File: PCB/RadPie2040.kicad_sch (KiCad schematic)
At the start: 42 parts, among them J1 USB_C_Receptacle_USB2.0, J2 SWD, J6 Conn_01x16, J7 Conn_01x16, SW1 SW_BOOTSEL, SW2 SW_RESET, U1 W25Q128JVSIQ, U2 RP2040, U4 XC6206PxxxMR-Regulator_Linear, X1 12MHz

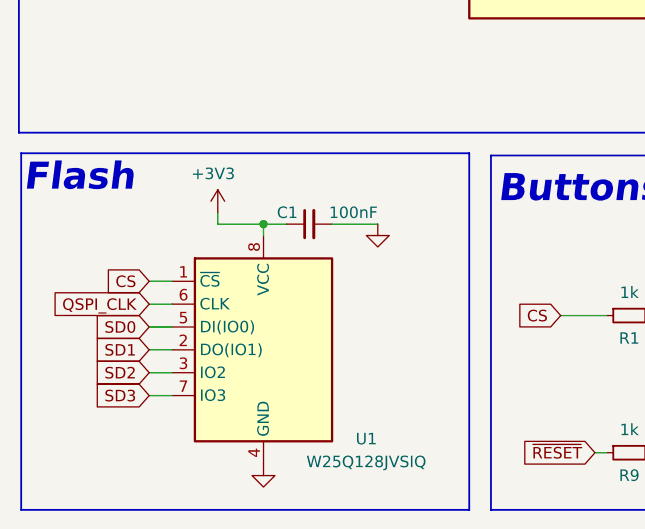
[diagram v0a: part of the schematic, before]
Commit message: Add pull-up for Flash, just in case
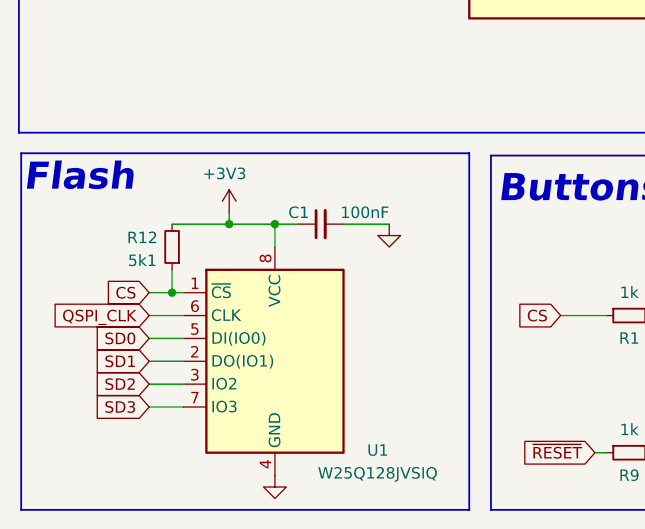
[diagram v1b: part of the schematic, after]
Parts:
- added R12: 5k1, Resistor_SMD:R_0402_1005Metric, symbol Device:R_Small
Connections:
- net +3V3: now also R12.2
- net CS: now also R12.1
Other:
- moved on the sheet: C1, U1

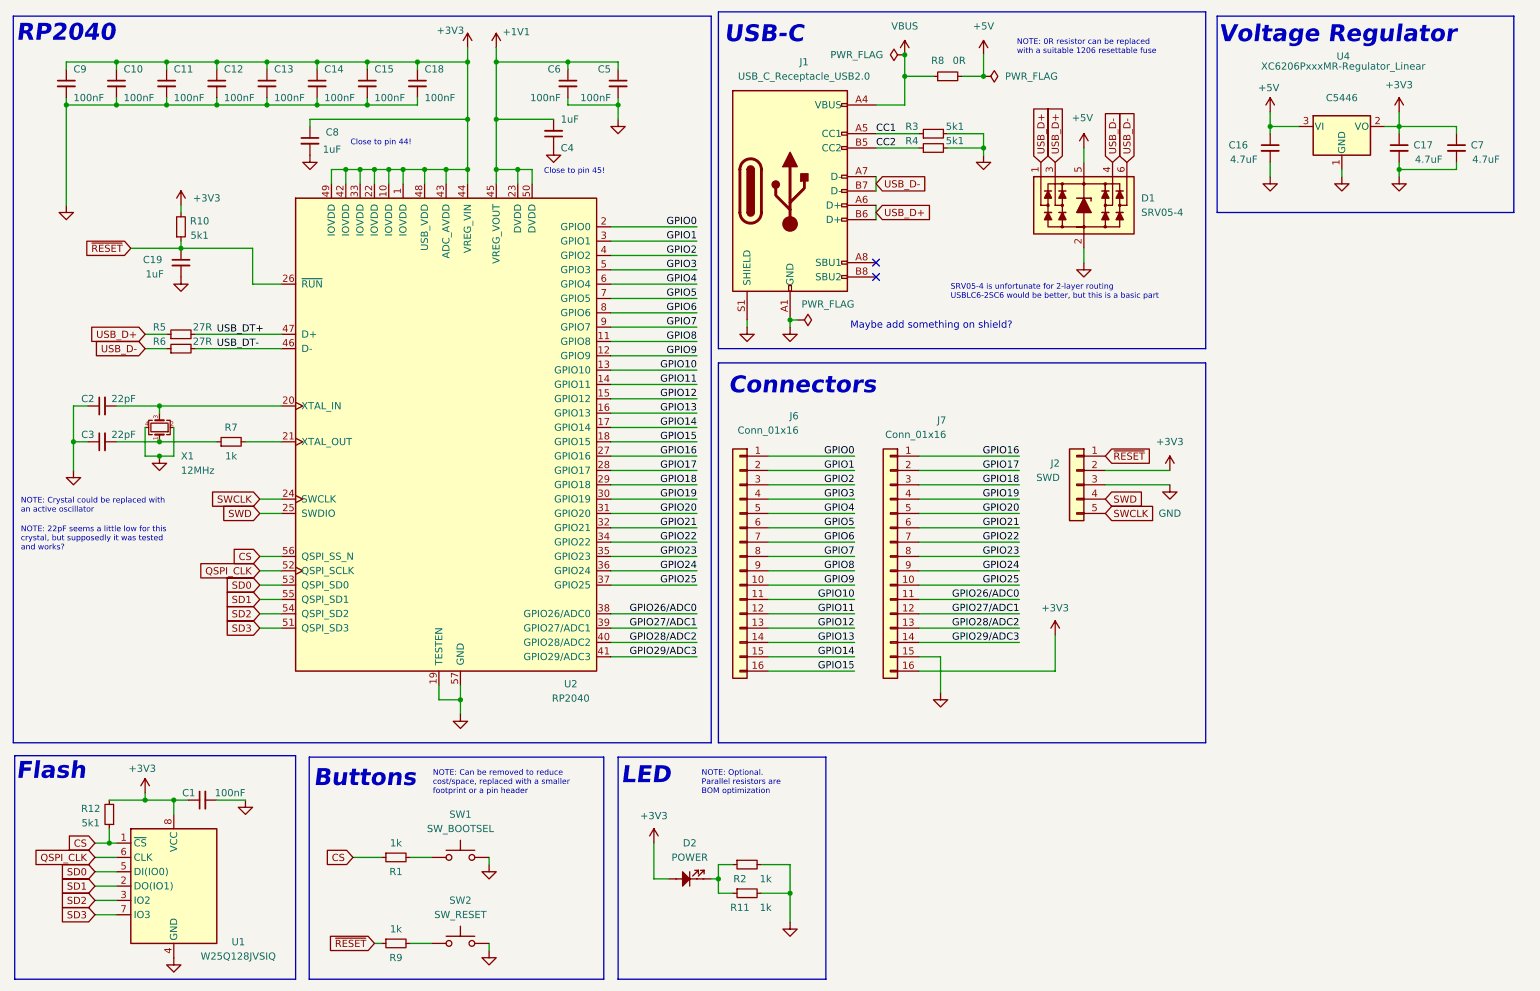
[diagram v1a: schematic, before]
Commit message: Refactor schematic to be hierarchical
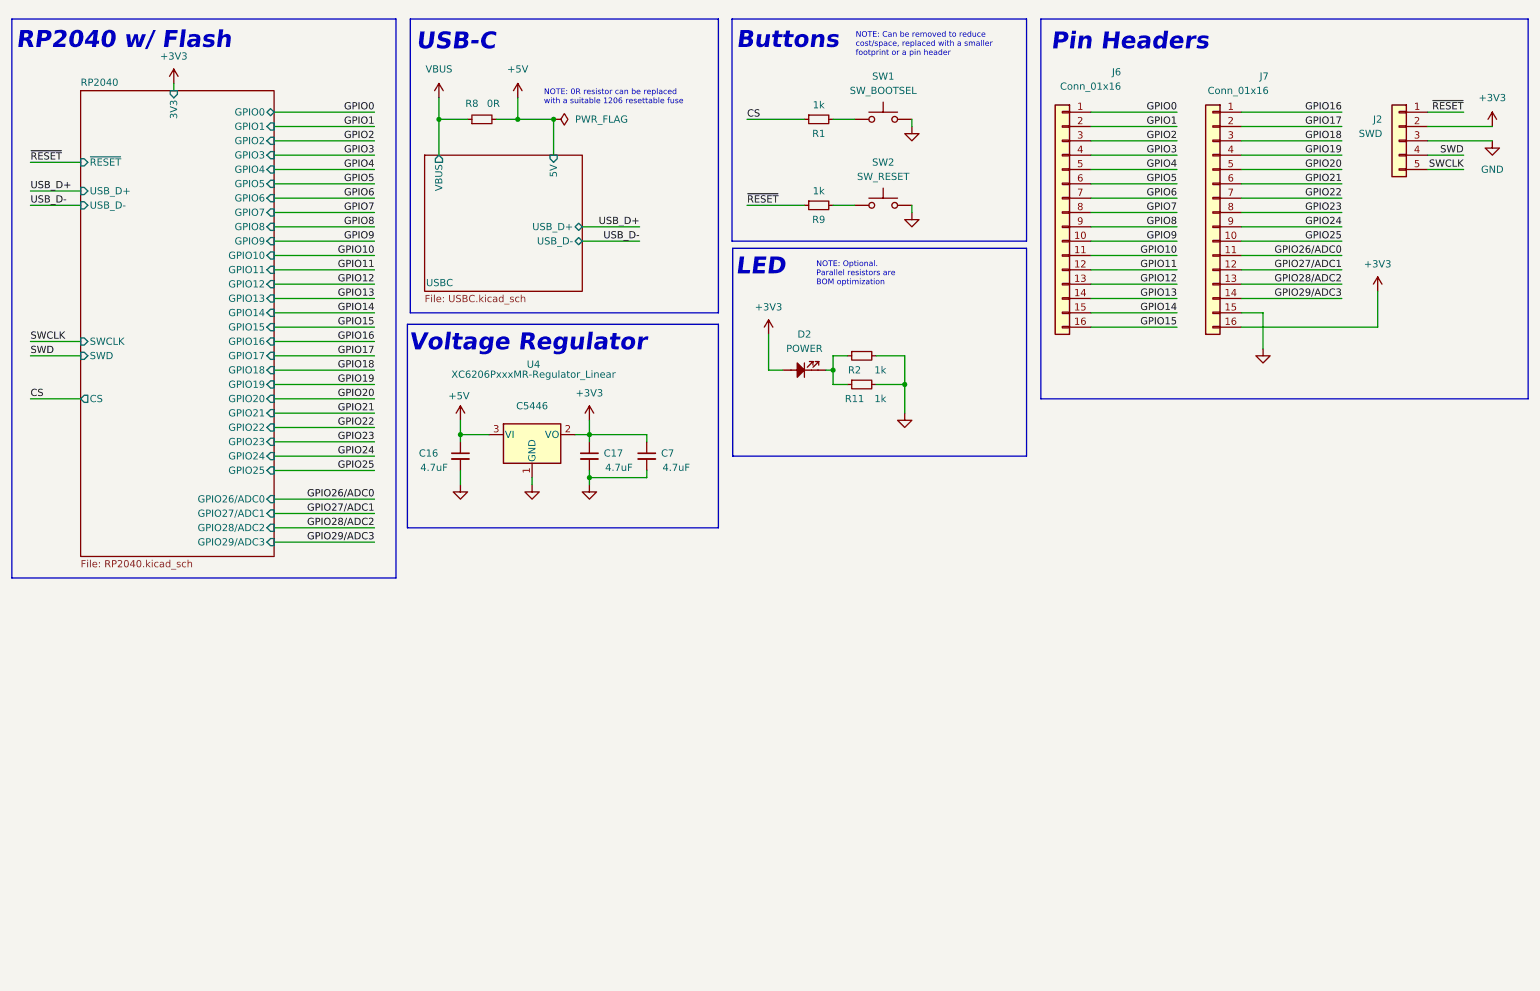
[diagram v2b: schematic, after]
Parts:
- removed C1, C10, C11, C12, C13, C14, C15, C18, C5, C6, C9: 100nF, Capacitor_SMD:C_0402_1005Metric, symbol Device:C_Small
- removed C19, C4, C8: 1uF, Capacitor_SMD:C_0402_1005Metric, symbol Device:C_Small
- removed C2, C3: 22pF, Capacitor_SMD:C_0402_1005Metric, symbol Device:C_Small
- removed D1: SRV05-4, Package_TO_SOT_SMD:SOT-23-6, symbol PCM_Diode_TVS_AKL:SRV05-4
- removed J1: USB_C_Receptacle_USB2.0, Connector_USB:USB_C_Receptacle_HRO_TYPE-C-31-M-12, symbol Connector:USB_C_Receptacle_USB2.0
- removed R10, R12, R3, R4: 5k1, Resistor_SMD:R_0402_1005Metric, symbol Device:R_Small
- removed R5, R6: 27R, Resistor_SMD:R_0603_1608Metric, symbol Device:R_Small
- removed R7: 1k, Resistor_SMD:R_0402_1005Metric, symbol Device:R_Small
- removed U1: W25Q128JVSIQ, Package_SO:SOIC-8_5.23x5.23mm_P1.27mm, symbol Memory_Flash:W25Q128JVS
- removed U2: RP2040, RadPie2040:RP2040-QFN-56, symbol RadPie2040:RP2040
- removed X1: 12MHz, Crystal:Crystal_SMD_3225-4Pin_3.2x2.5mm, symbol Device:Crystal_GND24_Small
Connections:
- no-connect marks 2 -> 0
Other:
- added sheet RP2040 (RP2040.kicad_sch)
- added sheet USBC (USBC.kicad_sch)
- note added: "Pin Headers"
- note added: "RP2040 w/ Flash"
- note removed: "Connectors"
- note removed: "Flash"
- note removed: "Maybe add something on shield?"
- note removed: "RP2040"
- note removed: "SRV05-4 is unfortunate for 2-layer routing USBLC6-2SC6 would be better, but this is a basic part"
- moved on the sheet: C16, C17, C7, D2, J2, J6, J7, R1, R11, R2, R9, SW1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
